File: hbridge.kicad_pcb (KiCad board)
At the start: 2 copper layers, 33 x 30.5 mm, 18 parts, among them J1 Conn_01x04_Male, J2 Screw_Terminal_01x03, Q1 2N7000, Q2 2N7000, Q3 2N3904, Q4 2N3906, Q5 2N3904, Q6 2N3906, Q7 STP20NF06, Q8 STP20NF06

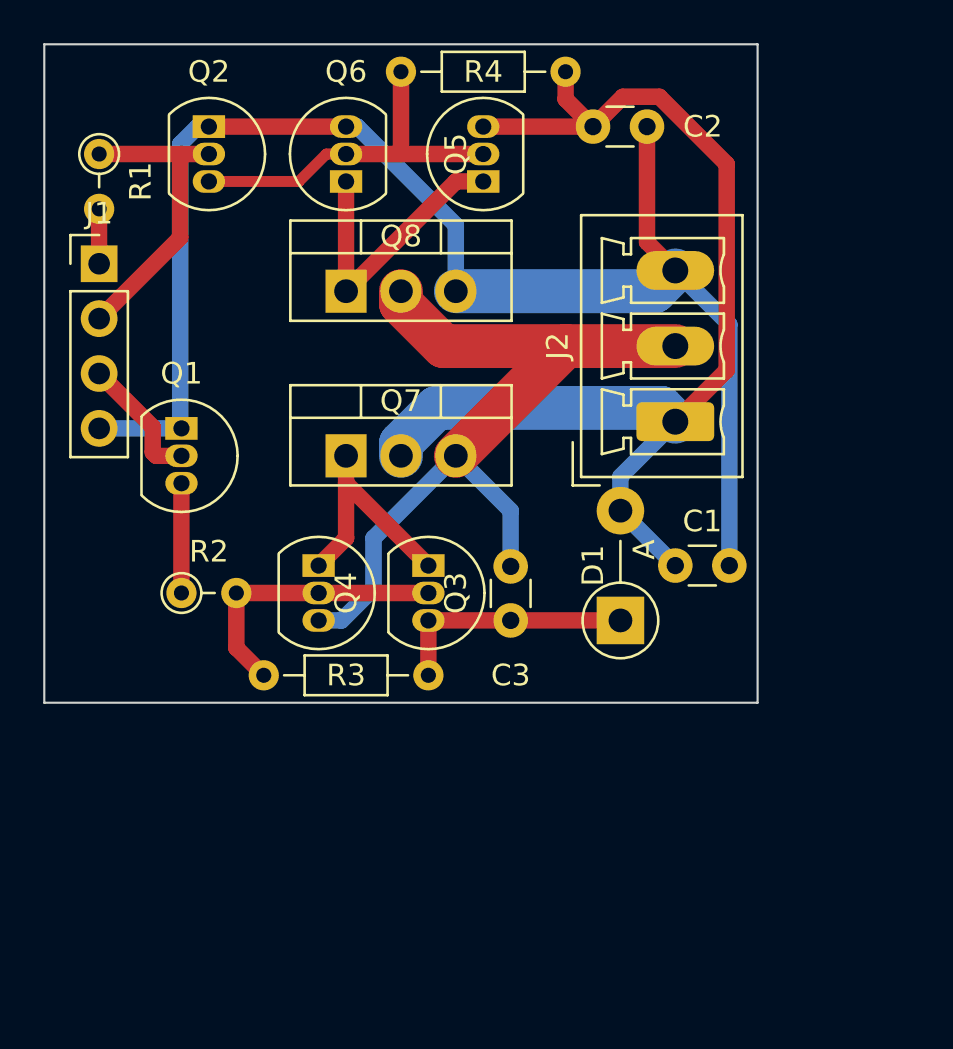
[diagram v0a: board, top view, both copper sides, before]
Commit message: Improved proto layout, snapped to 100 mil
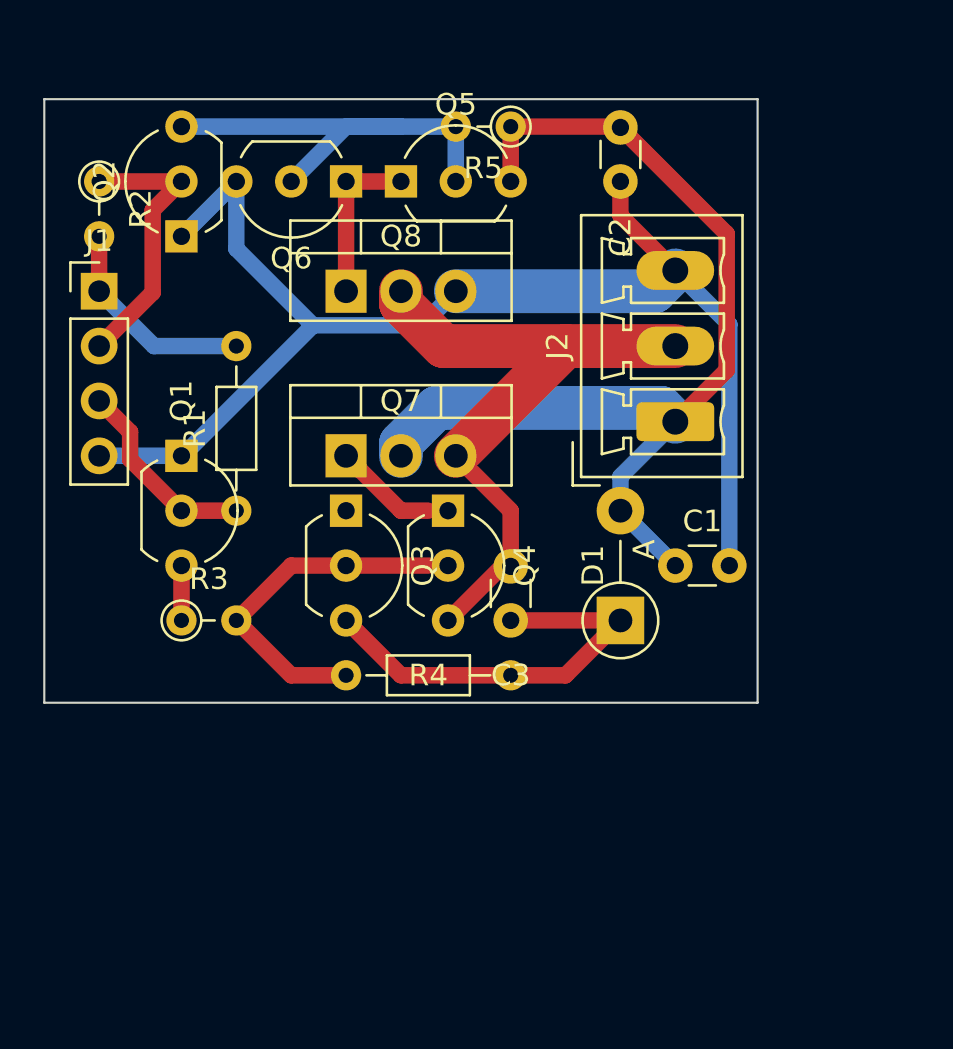
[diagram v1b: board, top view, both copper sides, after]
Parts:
- added R1: 100k, Resistor_THT:R_Axial_DIN0204_L3.6mm_D1.6mm_P7.62mm_Horizontal, F.Cu at (104.1, 71.1)
- Q1, Q2, Q3, Q4, Q5, Q6: footprint Package_TO_SOT_THT:TO-92_Inline -> Package_TO_SOT_THT:TO-92_Inline_Wide
- R5: renamed from R4; footprint Resistor_THT:R_Axial_DIN0204_L3.6mm_D1.6mm_P7.62mm_Horizontal -> Resistor_THT:R_Axial_DIN0204_L3.6mm_D1.6mm_P2.54mm_Vertical
- moved Q4 6.51 mm to (113.9, 71.1)
- moved Q2 5.24 mm to (101.6, 58.4), turned to 90 degrees
- moved Q3 4.58 mm to (109.2, 71.1)
- moved R4 3.81 mm to (116.8, 78.7)
- moved Q5 3.81 mm to (111.8, 55.9), turned to 0 degrees
- moved R5 3.59 mm to (116.8, 53.3)
- moved C2 1.27 mm to (121.9, 53.4), turned to -90 degrees
- moved J1 1.27 mm to (97.8, 61.0)
- moved R2 1.27 mm to (97.8, 55.9)
- moved Q1 1.27 mm to (101.6, 68.6)
- moved R3 1.27 mm to (101.6, 76.2)
- turned Q6 to 180 degrees
- renumbered R1 to R2, R2 to R3, R3 to R4
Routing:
- net /boot: track 11.4 -> 19.9 mm
- net +5V: track 2.54 -> 9.94 mm
- net /Vout: track 38.3 -> 31.4 mm
- net /drvH: track 11.0 -> 4.86 mm
- net /drvL: track 13.5 -> 7.62 mm
- net GND: track 67.5 -> 61.8 mm
- net +12V: track 52.1 -> 47.2 mm
- net Net-(Q2-Pad3): track 17.0 -> 21.4 mm
- net /PWM: track 6.07 -> 9.20 mm
- net Net-(Q3-Pad2): track 13.2 -> 16.1 mm
- net Net-(Q1-Pad3): track 5.08 -> 2.54 mm
- net /~PWM~: track 14.3 -> 13.0 mm
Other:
- board size 33 x 30.5 mm -> 33 x 27.9 mm

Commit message: Reduce layout to 1x1 inch, cleaned up silkscreen
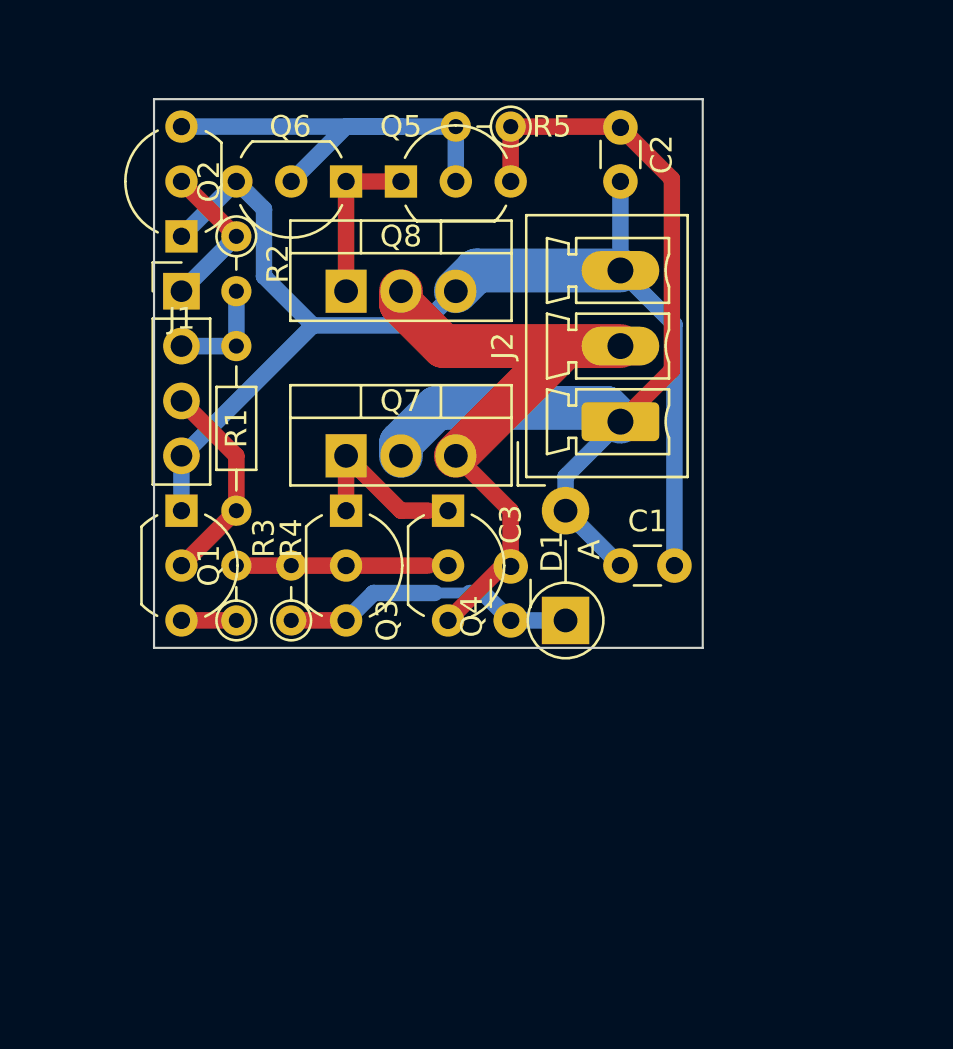
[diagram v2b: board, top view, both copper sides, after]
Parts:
- R4: footprint Resistor_THT:R_Axial_DIN0204_L3.6mm_D1.6mm_P7.62mm_Horizontal -> Resistor_THT:R_Axial_DIN0204_L3.6mm_D1.6mm_P2.54mm_Vertical
- moved R4 10.5 mm to (106.7, 76.2), turned to 90 degrees
- moved R2 6.84 mm to (104.1, 58.4)
- moved J1 3.81 mm to (101.6, 61.0)
- moved D1 2.54 mm to (119.4, 76.2)
- moved Q1 2.54 mm to (101.6, 71.1)
- moved R3 2.54 mm to (104.1, 76.2), turned to 90 degrees
- moved C1 2.54 mm to (121.9, 73.7)
- moved J2 2.54 mm to (121.9, 67.0)
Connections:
- J1 pad 1: +5V -> /~PWM~
- J1 pad 2: /~PWM~ -> +5V
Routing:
- net Net-(Q3-Pad2): track 16.1 -> 8.89 mm
- net /boot: track 19.9 -> 13.8 mm
- net /~PWM~: track 13.0 -> 7.18 mm
- net +5V: track 9.94 -> 5.08 mm
- net GND: track 61.8 -> 57.0 mm
- net +12V: track 47.2 -> 43.7 mm
- net /drvH: track 4.86 -> 7.40 mm
- net /Vout: track 31.4 -> 28.8 mm
- net /PWM: track 9.20 -> 9.72 mm
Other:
- board size 33 x 27.9 mm -> 25.4 x 25.4 mm

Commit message: Reduced the unique parts count by consolidating resistors and capacitors
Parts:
- C2: value 0.1u -> 1u
- R1, R2: value 100k -> 10k
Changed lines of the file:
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@@
       (effects (font (size 1 1) (thickness 0.15)))
     )
-    (fp_text value "100k" (at 3.81 1.92 90) (layer "F.Fab")
+    (fp_text value "10k" (at 3.81 1.92 90) (layer "F.Fab")
       (effects (font (size 1 1) (thickness 0.15)))
     )
@@
       (effects (font (size 1 1) (thickness 0.15)))
     )
-    (fp_text value "0.1u" (at 1.25 2.05 90) (layer "F.Fab")
+    (fp_text value "1u" (at 1.25 2.05 90) (layer "F.Fab")
       (effects (font (size 1 1) (thickness 0.15)))
     )
@@
       (effects (font (size 1 1) (thickness 0.15)))
     )
-    (fp_text value "100k" (at 1.27 1.92 90) (layer "F.Fab")
-      (effects (font (size 1 1) (thickness 0.15)))
-    )
+    (fp_text value "10k" (at 1.27 1.92 90) (layer "F.Fab")
+      (effects (font (size 1 1) (thickness 0.15)))
+    )

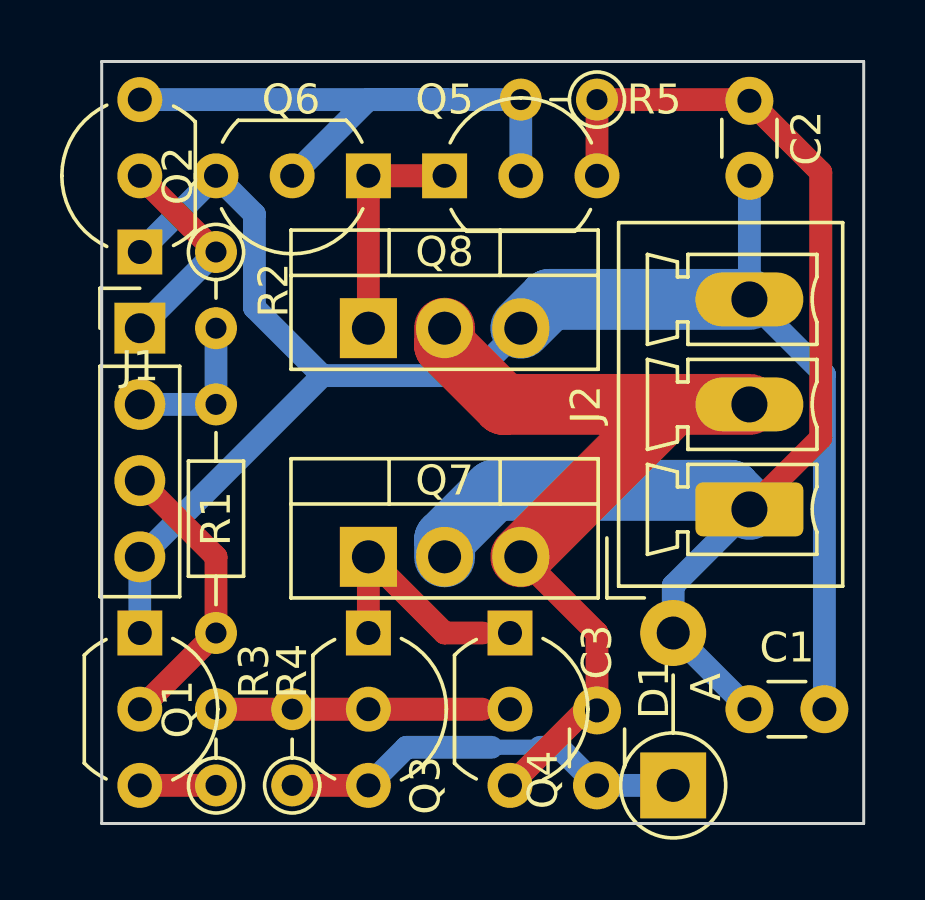
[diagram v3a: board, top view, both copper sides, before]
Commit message: Tied Q4 collector to ground to turn off Q7 harder. Moved traces so entire back side is ground plane.
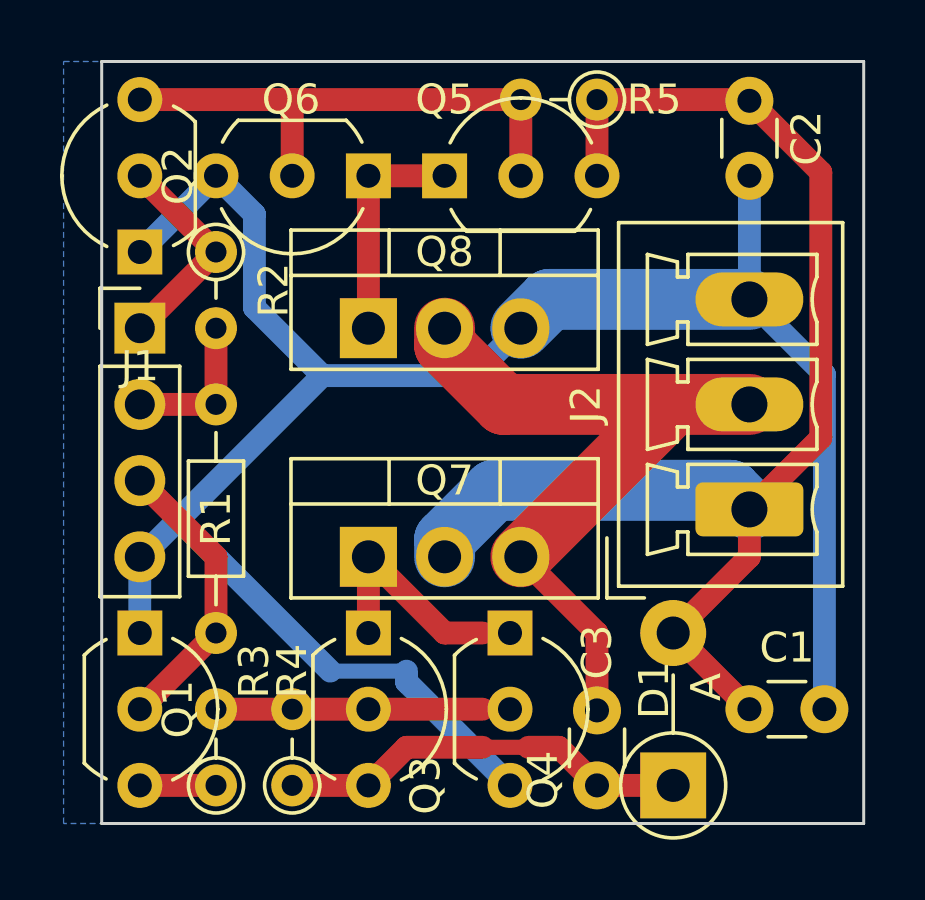
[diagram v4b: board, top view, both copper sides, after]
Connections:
- Q4 pad 3: /Vout -> GND
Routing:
- net GND: track 57.0 -> 71.9 mm
- net /Vout: track 28.8 -> 24.9 mm
- net Net-(Q2-Pad3): track 21.4 -> 19.1 mm
- added copper zone on B.Cu, net GND
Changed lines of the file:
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@@
       (net 9 "Net-(Q3-Pad2)") (pinfunction "B") (pintype "input"))
     (pad "3" thru_hole circle (at 5.08 0 270) (size 1.5 1.5) (drill 0.8) (layers *.Cu *.Mask)
-      (net 3 "/Vout") (pinfunction "C") (pintype "passive"))
+      (net 2 "GND") (pinfunction "C") (pintype "passive"))
     (model "${KICAD6_3DMODEL_DIR}/Package_TO_SOT_THT.3dshapes/TO-92_Inline_Wide.wrl"
       (offset (xyz 0 0 0))
@@
   (segment (start 116.84 53.34) (end 116.84 55.88) (width 0.762) (layer "F.Cu") (net 1))
   (segment (start 116.84 53.34) (end 121.92 53.34) (width 0.762) (layer "F.Cu") (net 1))
+  (segment (start 119.38 71.12) (end 121.92 73.66) (width 0.762) (layer "F.Cu") (net 1))
   (segment (start 124.30052 55.76052) (end 124.30052 64.61948) (width 0.762) (layer "F.Cu") (net 1))
   (segment (start 124.30052 64.61948) (end 121.92 67) (width 0.762) (layer "F.Cu") (net 1))
+  (segment (start 121.92 68.58) (end 119.38 71.12) (width 0.762) (layer "F.Cu") (net 1))
   (segment (start 121.92 53.38) (end 124.30052 55.76052) (width 0.762) (layer "F.Cu") (net 1))
+  (segment (start 121.92 67) (end 121.92 68.58) (width 0.762) (layer "F.Cu") (net 1))
   (segment (start 113.401977 66.36448) (end 111.76 68.006457) (width 2.032) (layer "B.Cu") (net 1))
-  (segment (start 121.92 73.66) (end 119.38 71.12) (width 0.762) (layer "B.Cu") (net 1))
   (segment (start 121.28448 66.36448) (end 113.401977 66.36448) (width 2.032) (layer "B.Cu") (net 1))
   (segment (start 111.76 68.006457) (end 111.76 68.58) (width 2.032) (layer "B.Cu") (net 1))
   (segment (start 121.92 67) (end 121.28448 66.36448) (width 2.032) (layer "B.Cu") (net 1))
-  (segment (start 119.38 71.12) (end 119.38 69.54) (width 0.762) (layer "B.Cu") (net 1))
-  (segment (start 119.38 69.54) (end 121.92 67) (width 0.762) (layer "B.Cu") (net 1))
   (segment (start 104.14 55.88) (end 105.420511 57.160511) (width 0.762) (layer "B.Cu") (net 2))
+  (segment (start 113.94 76.2) (end 110.49 72.75) (width 0.762) (layer "B.Cu") (net 2))
   (segment (start 104.14 55.88) (end 101.6 58.42) (width 0.762) (layer "B.Cu") (net 2))
   (segment (start 124.42 62.5) (end 121.92 60) (width 0.762) (layer "B.Cu") (net 2))
   (segment (start 105.420511 57.160511) (end 105.420511 60.274033) (width 0.762) (layer "B.Cu") (net 2))
-  (segment (start 101.6475 68.58) (end 107.686989 62.540511) (width 0.762) (layer "B.Cu") (net 2))
   (segment (start 121.92 55.88) (end 121.92 60) (width 0.762) (layer "B.Cu") (net 2))
   (segment (start 112.719489 62.540511) (end 114.3 60.96) (width 0.762) (layer "B.Cu") (net 2))
@@
   (segment (start 115.26 60) (end 114.3 60.96) (width 2.032) (layer "B.Cu") (net 2))
   (segment (start 105.420511 60.274033) (end 107.686989 62.540511) (width 0.762) (layer "B.Cu") (net 2))
+  (segment (start 102.89375 67.33375) (end 107.686989 62.540511) (width 0.762) (layer "B.Cu") (net 2))
   (segment (start 124.42 73.66) (end 124.42 62.5) (width 0.762) (layer "B.Cu") (net 2))
+  (segment (start 110.49 72.75) (end 110.49 72.39) (width 0.762) (layer "B.Cu") (net 2))
+  (segment (start 110.49 72.39) (end 107.95 72.39) (width 0.508) (layer "B.Cu") (net 2))
+  (segment (start 107.95 72.39) (end 102.89375 67.33375) (width 0.762) (layer "B.Cu") (net 2))
+  (segment (start 101.6475 68.58) (end 102.89375 67.33375) (width 0.762) (layer "B.Cu") (net 2))
   (segment (start 107.686989 62.540511) (end 112.719489 62.540511) (width 0.762) (layer "B.Cu") (net 2))
   (segment (start 101.6 68.58) (end 101.6 71.12) (width 0.762) (layer "B.Cu") (net 2))
@@
   (segment (start 119.38 63.5) (end 114.3 68.58) (width 2.032) (layer "F.Cu") (net 3))
   (segment (start 111.76 61.533543) (end 113.726457 63.5) (width 2.032) (layer "F.Cu") (net 3))
-  (segment (start 116.84 73.7) (end 116.44 73.7) (width 0.762) (layer "F.Cu") (net 3))
-  (segment (start 116.44 73.7) (end 113.94 76.2) (width 0.762) (layer "F.Cu") (net 3))
-  (segment (start 101.6 63.5) (end 104.14 63.5) (width 0.762) (layer "B.Cu") (net 4))
-  (segment (start 104.14 60.96) (end 104.14 63.5) (width 0.762) (layer "B.Cu") (net 4))
+  (segment (start 101.6 63.5) (end 104.14 63.5) (width 0.762) (layer "F.Cu") (net 4))
+  (segment (start 104.14 63.5) (end 104.14 60.96) (width 0.762) (layer "F.Cu") (net 4))
   (segment (start 104.14 71.12) (end 104.14 68.58) (width 0.762) (layer "F.Cu") (net 5))
   (segment (start 101.6 73.66) (end 104.14 71.12) (width 0.762) (layer "F.Cu") (net 5))
   (segment (start 104.14 68.58) (end 101.6 66.04) (width 0.762) (layer "F.Cu") (net 5))
   (segment (start 101.6 55.88) (end 104.14 58.42) (width 0.762) (layer "F.Cu") (net 6))
-  (segment (start 101.6 60.96) (end 104.14 58.42) (width 0.762) (layer "B.Cu") (net 6))
+  (segment (start 101.6 60.96) (end 104.14 58.42) (width 0.762) (layer "F.Cu") (net 6))
   (segment (start 101.6 76.2) (end 104.14 76.2) (width 0.762) (layer "F.Cu") (net 7))
-  (segment (start 114.3 53.34) (end 114.3 55.88) (width 0.762) (layer "B.Cu") (net 8))
-  (segment (start 111.76 53.34) (end 114.3 53.34) (width 0.762) (layer "B.Cu") (net 8))
-  (segment (start 106.68 55.88) (end 109.22 53.34) (width 0.762) (layer "B.Cu") (net 8))
-  (segment (start 109.22 53.34) (end 111.76 53.34) (width 0.762) (layer "B.Cu") (net 8))
-  (segment (start 101.6 53.34) (end 111.76 53.34) (width 0.762) (layer "B.Cu") (net 8))
+  (segment (start 106.68 53.34) (end 105.41 53.34) (width 0.762) (layer "F.Cu") (net 8))
+  (segment (start 114.3 55.88) (end 114.3 53.34) (width 0.762) (layer "F.Cu") (net 8))
+  (segment (start 114.3 53.34) (end 105.41 53.34) (width 0.762) (layer "F.Cu") (net 8))
+  (segment (start 106.68 55.88) (end 106.68 53.34) (width 0.762) (layer "F.Cu") (net 8))
+  (segment (start 105.41 53.34) (end 101.6 53.34) (width 0.762) (layer "F.Cu") (net 8))
   (segment (start 104.14 73.66) (end 106.68 73.66) (width 0.762) (layer "F.Cu") (net 9))
   (segment (start 106.68 73.66) (end 113.03 73.66) (width 0.762) (layer "F.Cu") (net 9))
+  (segment (start 110.49 74.93) (end 109.22 76.2) (width 0.762) (layer "F.Cu") (net 10))
+  (segment (start 119.38 76.2) (end 116.84 76.2) (width 0.762) (layer "F.Cu") (net 10))
   (segment (start 106.68 76.2) (end 109.22 76.2) (width 0.762) (layer "F.Cu") (net 10))
-  (segment (start 109.22 76.2) (end 110.49 74.93) (width 0.762) (layer "B.Cu") (net 10))
-  (segment (start 119.38 76.2) (end 116.84 76.2) (width 0.762) (layer "B.Cu") (net 10))
-  (segment (start 110.49 74.93) (end 113.328372 74.93) (width 0.762) (layer "B.Cu") (net 10))
-  (segment (start 116.84 76.2) (end 115.57 74.93) (width 0.762) (layer "B.Cu") (net 10))
-  (segment (start 115.57 74.93) (end 114.935 74.93) (width 0.762) (layer "B.Cu") (net 10))
-  (segment (start 113.328372 74.93) (end 114.935 74.93) (width 0.508) (layer "B.Cu") (net 10))
+  (segment (start 113.03 74.93) (end 110.49 74.93) (width 0.762) (layer "F.Cu") (net 10))
+  (segment (start 116.84 76.2) (end 115.57 74.93) (width 0.762) (layer "F.Cu") (net 10))
+  (segment (start 115.57 74.93) (end 114.551628 74.93) (width 0.762) (layer "F.Cu") (net 10))
+  (segment (start 114.551628 74.93) (end 113.03 74.93) (width 0.508) (layer "F.Cu") (net 10))
   (segment (start 109.22 68.58) (end 111.76 71.12) (width 0.762) (layer "F.Cu") (net 11))
   (segment (start 111.76 71.12) (end 113.03 71.12) (width 0.762) (layer "F.Cu") (net 11))
@@
   (segment (start 109.22 55.88) (end 111.76 55.88) (width 0.762) (layer "F.Cu") (net 12))
   (segment (start 109.22 60.96) (end 109.22 55.88) (width 0.762) (layer "F.Cu") (net 12))
+  (zone (net 2) (net_name "GND") (layer "B.Cu") (hatch edge 0.508)
+    (connect_pads (clearance 0.508))
+    (min_thickness 0.254) (filled_areas_thickness no)
+    (fill yes (thermal_gap 0.508) (thermal_bridge_width 0.508))
+    (polygon
+      (pts
+        (xy 125.73 77.47)
+        (xy 99.06 77.47)
+        (xy 99.06 52.07)
+        (xy 125.73 52.07)
+      )
+    )
+  )
 )

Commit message: Removed R3 to turn off Q7 harder
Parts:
- removed R3: 10k, Resistor_THT:R_Axial_DIN0204_L3.6mm_D1.6mm_P2.54mm_Vertical
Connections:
- Q1 pad 3: Net-(Q1-Pad3) -> Net-(Q3-Pad2)
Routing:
- net Net-(Q3-Pad2): track 8.89 -> 12.5 mm
- net Net-(Q1-Pad3): track 2.54 -> 0.00 mm
